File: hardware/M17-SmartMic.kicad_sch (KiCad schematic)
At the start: 0 parts

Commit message: Updated schematic title block
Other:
- company: (none) -> M17Project
- title: (none) -> Module17
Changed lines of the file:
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@@
 (kicad_sch (version 20230121) (generator eeschema)
   (paper "A4")
+  (title_block
+    (title "Module17")
+    (date "2023-07-18")
+    (rev "Rev 1.0")
+    (company "M17Project")
+    (comment 1 "Mathis - DB9MAT")
+    (comment 2 "Wojciech - SP5WWP")
+    (comment 3 "Authors:")
+  )
   (sheet (at 25.4 26.67) (size 25.4 13.97) (fields_autoplaced)
     (stroke (width 0) (type solid))

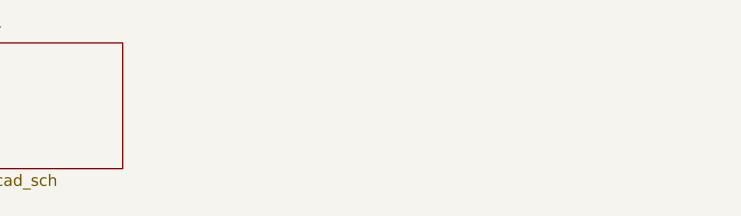
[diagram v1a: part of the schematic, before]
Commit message: Reworked audio output diagram
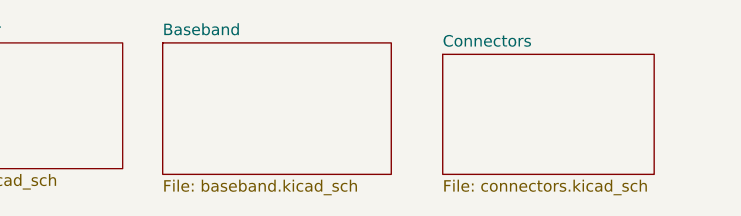
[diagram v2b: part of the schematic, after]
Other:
- added sheet Baseband (baseband.kicad_sch)
- added sheet Connectors (connectors.kicad_sch)
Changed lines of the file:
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@@
+    )
+  )
+  (sheet (at 93.345 26.67) (size 25.4 14.605) (fields_autoplaced)
+    (stroke (width 0.1524) (type solid))
+    (fill (color 0 0 0 0.0000))
+    (property "Sheetname" "Baseband" (at 93.345 25.9584 0)
+      (effects (font (size 1.27 1.27)) (justify left bottom))
+    )
+    (property "Sheetfile" "baseband.kicad_sch" (at 93.345 41.8596 0)
+      (effects (font (size 1.27 1.27)) (justify left top))
+    )
+    (instances
+      (project "M17-SmartMic"
+        (path "/59592280-3207-432b-a891-cd517ec5cf12" (page "5"))
+      )
+    )
+  )
+  (sheet (at 124.46 27.94) (size 23.495 13.335) (fields_autoplaced)
+    (stroke (width 0.1524) (type solid))
+    (fill (color 0 0 0 0.0000))
+    (property "Sheetname" "Connectors" (at 124.46 27.2284 0)
+      (effects (font (size 1.27 1.27)) (justify left bottom))
+    )
+    (property "Sheetfile" "connectors.kicad_sch" (at 124.46 41.8596 0)
+      (effects (font (size 1.27 1.27)) (justify left top))
+    )
+    (instances
+      (project "M17-SmartMic"
+        (path "/59592280-3207-432b-a891-cd517ec5cf12" (page "4"))
+      )
     )
   )

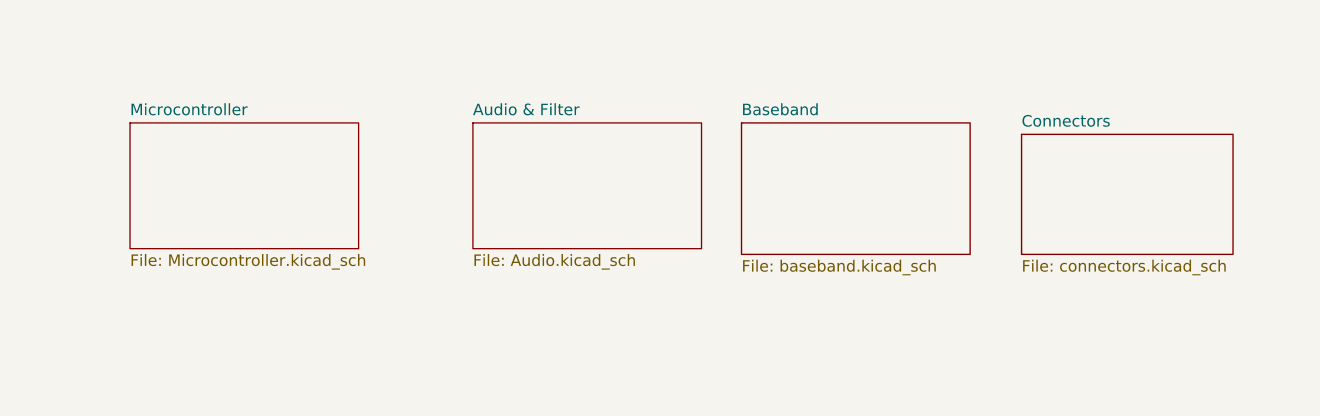
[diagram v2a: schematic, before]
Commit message: Reworked schematic
Rearranged disposition and renumbered components
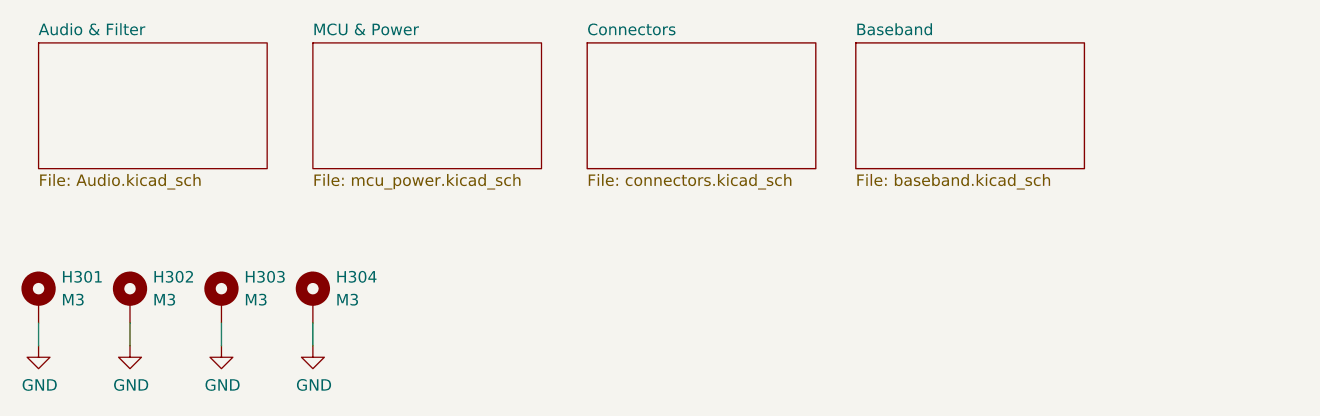
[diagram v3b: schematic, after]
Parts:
- added H301, H302, H303, H304: M3, MountingHole:MountingHole_2.7mm_M2.5_DIN965_Pad, symbol Mechanical:MountingHole_Pad
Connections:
- new net GND: H301.1, H302.1, H303.1, H304.1
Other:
- sheet Microcontroller renamed MCU & Power
- sheet MCU & Power: file Microcontroller.kicad_sch -> mcu_power.kicad_sch

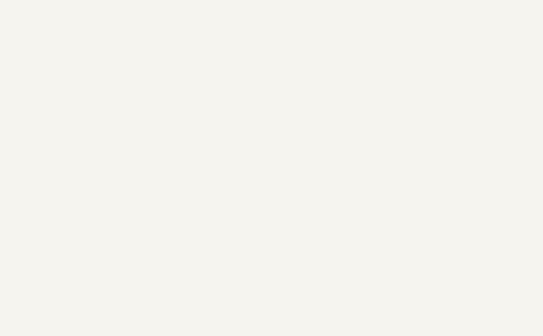
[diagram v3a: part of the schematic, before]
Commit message: Updated logos in schematic
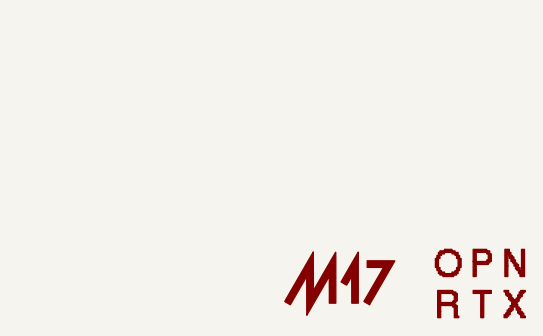
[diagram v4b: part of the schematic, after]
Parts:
- added LOGO101: M17_logo, M17_logos:M17_logo_20x11.5mm, symbol M17_logos:M17_logo
- added U101: ~, M17_logos:OPN_RTX_logo_10x7.6mm, symbol M17_logos:OPN_RTX_logo
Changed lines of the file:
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@@
+    )
+  )
+  (symbol (lib_id "M17_logos:OPN_RTX_logo") (at 240.665 174.625 0) (unit 1)
+    (in_bom no) (on_board yes) (dnp no) (fields_autoplaced)
+    (property "Reference" "U101" (at 240.665 174.625 0)
+      (effects (font (size 1.27 1.27)) hide)
+    )
+    (property "Value" "~" (at 240.665 174.625 0)
+      (effects (font (size 1.27 1.27)))
+    )
+    (property "Footprint" "M17_logos:OPN_RTX_logo_10x7.6mm" (at 240.665 174.625 0)
+      (effects (font (size 1.27 1.27)) hide)
+    )
+    (property "Datasheet" "" (at 240.665 174.625 0)
+      (effects (font (size 1.27 1.27)) hide)
+    )
+    (instances
+      (project "M17-SmartMic"
+        (path "/59592280-3207-432b-a891-cd517ec5cf12"
+          (reference "U101") (unit 1)
+        )
+      )
     )
   )
@@
         )
       )
+    )
+  )
+  (symbol (lib_id "M17_logos:M17_logo") (at 224.79 174.625 0) (unit 1)
+    (in_bom no) (on_board yes) (dnp no) (fields_autoplaced)
+    (property "Reference" "LOGO101" (at 224.79 169.799 0)
+      (effects (font (size 1.27 1.27)) hide)
+    )
+    (property "Value" "M17_logo" (at 224.79 169.672 0)
+      (effects (font (size 1.27 1.27)) hide)
+    )
+    (property "Footprint" "M17_logos:M17_logo_20x11.5mm" (at 221.615 172.339 0)
+      (effects (font (size 1.27 1.27)) hide)
+    )
+    (property "Datasheet" "" (at 221.615 172.339 0)
+      (effects (font (size 1.27 1.27)) hide)
+    )
+    (instances
+      (project "M17-SmartMic"
+        (path "/59592280-3207-432b-a891-cd517ec5cf12"
+          (reference "LOGO101") (unit 1)
+        )
+      )

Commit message: Updated existing logos
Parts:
- LOGO102: renamed from U101; value ~ -> OPN_RTX_logo
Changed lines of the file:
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@@
   (symbol (lib_id "M17_logos:OPN_RTX_logo") (at 240.665 174.625 0) (unit 1)
     (in_bom no) (on_board yes) (dnp no) (fields_autoplaced)
-    (property "Reference" "U101" (at 240.665 174.625 0)
+    (property "Reference" "LOGO102" (at 240.665 174.625 0)
       (effects (font (size 1.27 1.27)) hide)
     )
-    (property "Value" "~" (at 240.665 174.625 0)
-      (effects (font (size 1.27 1.27)))
+    (property "Value" "OPN_RTX_logo" (at 240.665 174.625 0)
+      (effects (font (size 1.27 1.27)) hide)
     )
     (property "Footprint" "M17_logos:OPN_RTX_logo_10x7.6mm" (at 240.665 174.625 0)
@@
       (project "M17-SmartMic"
         (path "/59592280-3207-432b-a891-cd517ec5cf12"
-          (reference "U101") (unit 1)
+          (reference "LOGO102") (unit 1)
         )
       )

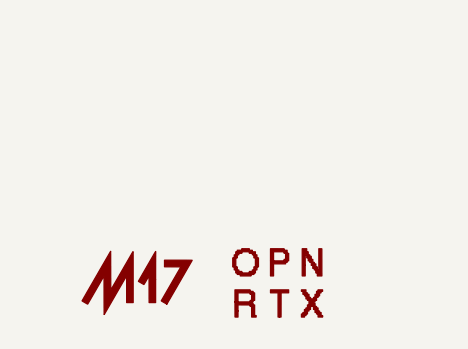
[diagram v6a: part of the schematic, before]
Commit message: Updated OSHW logo
Added OSHW logo to schematic, updated board logo
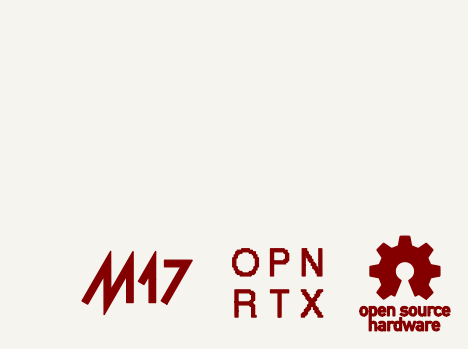
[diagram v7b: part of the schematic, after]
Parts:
- added LOGO103: OSHW_logo, M17_logos:OSHW_logo_12.5x13mm, symbol M17_logos:OSHW_logo
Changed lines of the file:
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@@
+    )
+  )
+  (symbol (lib_id "M17_logos:OSHW_logo") (at 254.635 174.625 0) (unit 1)
+    (in_bom no) (on_board yes) (dnp no) (fields_autoplaced)
+    (property "Reference" "LOGO103" (at 254.635 170.0012 0)
+      (effects (font (size 1.27 1.27)) hide)
+    )
+    (property "Value" "OSHW_logo" (at 254.635 179.2488 0)
+      (effects (font (size 1.27 1.27)) hide)
+    )
+    (property "Footprint" "M17_logos:OSHW_logo_12.5x13mm" (at 254.635 174.625 0)
+      (effects (font (size 1.27 1.27)) hide)
+    )
+    (property "Datasheet" "" (at 254.635 174.625 0)
+      (effects (font (size 1.27 1.27)) hide)
+    )
+    (instances
+      (project "M17-SmartMic"
+        (path "/59592280-3207-432b-a891-cd517ec5cf12"
+          (reference "LOGO103") (unit 1)
+        )
+      )
     )
   )
